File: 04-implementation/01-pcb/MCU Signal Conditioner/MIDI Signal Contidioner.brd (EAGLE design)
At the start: 78 x 31.9 mm, 26 parts, among them J2 ARDUINO-CONN-8X2, J3 ARDUINO-CONN-8X2, U4 24CS01, U6 MCP1700-SOT89, X1 SSW-107-02-S-D, X2 SSW-107-02-S-D, X3 SSW-107-02-S-D, X4 SSW-107-02-S-D, X5 MINI-USB-SHIELD-32005-201

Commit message: Update signal conditioner board.
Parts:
- moved C2 21.7 mm to (68.2, 21.8), turned to 270 degrees
- moved C1 8.01 mm to (48.4, 12.1)
- moved R9 2.04 mm to (26.2, 24.0)
- moved R7 2.03 mm to (26.2, 21.1)
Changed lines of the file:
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@@
 </element>
 <element name="U$2" library="MIDI Signal Conditioner Parts" package="74LVC4245A-SO24" value="74LVC4245A" x="56.896" y="16.129" rot="R180"/>
-<element name="C1" library="rcl" library_urn="urn:adsk.eagle:library:334" package="C0805" package3d_urn="urn:adsk.eagle:package:23617/2" value="100n" x="48.768" y="20.066" rot="R270"/>
-<element name="C2" library="rcl" library_urn="urn:adsk.eagle:library:334" package="C0805" package3d_urn="urn:adsk.eagle:package:23617/2" value="100n" x="48.768" y="12.192" rot="R90"/>
+<element name="C1" library="rcl" library_urn="urn:adsk.eagle:library:334" package="C0805" package3d_urn="urn:adsk.eagle:package:23617/2" value="100n" x="48.387" y="12.065" rot="R270"/>
+<element name="C2" library="rcl" library_urn="urn:adsk.eagle:library:334" package="C0805" package3d_urn="urn:adsk.eagle:package:23617/2" value="100n" x="68.199" y="21.844" rot="R270"/>
 <element name="R3" library="rcl" library_urn="urn:adsk.eagle:library:334" package="R0805W" package3d_urn="urn:adsk.eagle:package:23537/1" value="10K" x="19.177" y="21.082">
 <attribute name="SPICEPREFIX" value="R" x="19.177" y="21.082" size="1.778" layer="27" display="off"/>
@@
 <attribute name="SPICEPREFIX" value="R" x="43.561" y="11.557" size="1.778" layer="27" display="off"/>
 </element>
-<element name="R7" library="rcl" library_urn="urn:adsk.eagle:library:334" package="R0805W" package3d_urn="urn:adsk.eagle:package:23537/1" value="10K" x="24.13" y="21.082">
-<attribute name="SPICEPREFIX" value="R" x="24.13" y="21.082" size="1.778" layer="27" display="off"/>
+<element name="R7" library="rcl" library_urn="urn:adsk.eagle:library:334" package="R0805W" package3d_urn="urn:adsk.eagle:package:23537/1" value="10K" x="26.162" y="21.082">
+<attribute name="SPICEPREFIX" value="R" x="26.162" y="21.082" size="1.778" layer="27" display="off"/>
 </element>
 <element name="R8" library="rcl" library_urn="urn:adsk.eagle:library:334" package="R0805W" package3d_urn="urn:adsk.eagle:package:23537/1" value="20K" x="43.561" y="22.225">
 <attribute name="SPICEPREFIX" value="R" x="43.561" y="22.225" size="1.778" layer="27" display="off"/>
 </element>
-<element name="R9" library="rcl" library_urn="urn:adsk.eagle:library:334" package="R0805W" package3d_urn="urn:adsk.eagle:package:23537/1" value="10K" x="24.13" y="24.13">
-<attribute name="SPICEPREFIX" value="R" x="24.13" y="24.13" size="1.778" layer="27" display="off"/>
+<element name="R9" library="rcl" library_urn="urn:adsk.eagle:library:334" package="R0805W" package3d_urn="urn:adsk.eagle:package:23537/1" value="10K" x="26.162" y="24.003">
+<attribute name="SPICEPREFIX" value="R" x="26.162" y="24.003" size="1.778" layer="27" display="off"/>
 </element>
 <element name="R10" library="rcl" library_urn="urn:adsk.eagle:library:334" package="R0805W" package3d_urn="urn:adsk.eagle:package:23537/1" value="20K" x="43.561" y="15.113">
@@
 <contactref element="X4" pad="1"/>
 <contactref element="X4" pad="14"/>
-<wire x1="65.151" y1="20.729" x2="68.072" y2="29.464" width="0" layer="19" extent="1-1"/>
+<wire x1="68.199" y1="22.794" x2="68.072" y2="29.464" width="0" layer="19" extent="1-1"/>
+<wire x1="65.151" y1="20.729" x2="68.199" y2="22.794" width="0" layer="19" extent="1-1"/>
 <wire x1="77.343" y1="31.242" x2="68.072" y2="29.464" width="0" layer="19" extent="1-1"/>
 <wire x1="9.525" y1="26.797" x2="9.271" y2="23.048" width="0" layer="19" extent="1-1"/>
@@
 <wire x1="31.242" y1="26.924" x2="46.482" y2="29.464" width="0" layer="19" extent="1-1"/>
 <wire x1="24.765" y1="29.337" x2="31.242" y2="26.924" width="0" layer="19" extent="1-1"/>
-<wire x1="48.768" y1="11.242" x2="52.832" y2="26.924" width="0" layer="19" extent="1-1"/>
 </signal>
 <signal name="GND">
@@
 <contactref element="R6" pad="2"/>
 <contactref element="R4" pad="2"/>
-<wire x1="68.072" y1="26.924" x2="63.881" y2="20.729" width="0" layer="19" extent="1-1"/>
+<wire x1="63.881" y1="20.729" x2="68.199" y2="20.894" width="0" layer="19" extent="1-1"/>
+<wire x1="72.8619" y1="20.2641" x2="68.199" y2="20.894" width="0" layer="19" extent="1-1"/>
 <wire x1="21.854" y1="17.632" x2="19.177" y2="17.526" width="0" layer="19" extent="1-1"/>
 <wire x1="23.124" y1="17.632" x2="21.854" y2="17.632" width="0" layer="19" extent="1-1"/>
@@
 <wire x1="44.6135" y1="15.113" x2="44.6135" y2="18.669" width="0" layer="19" extent="1-1"/>
 <wire x1="44.6135" y1="11.557" x2="44.6135" y2="15.113" width="0" layer="19" extent="1-1"/>
-<wire x1="48.768" y1="19.116" x2="44.6135" y2="18.669" width="0" layer="19" extent="1-1"/>
-<wire x1="51.181" y1="20.729" x2="48.768" y2="19.116" width="0" layer="19" extent="1-1"/>
-<wire x1="52.451" y1="20.729" x2="51.181" y2="20.729" width="0" layer="19" extent="1-1"/>
-<wire x1="48.768" y1="13.142" x2="44.6135" y2="11.557" width="0" layer="19" extent="1-1"/>
-<wire x1="51.181" y1="11.529" x2="48.768" y2="13.142" width="0" layer="19" extent="1-1"/>
+<wire x1="48.387" y1="11.115" x2="44.6135" y2="11.557" width="0" layer="19" extent="1-1"/>
+<wire x1="51.181" y1="11.529" x2="48.387" y2="11.115" width="0" layer="19" extent="1-1"/>
 <wire x1="52.451" y1="11.529" x2="51.181" y2="11.529" width="0" layer="19" extent="1-1"/>
 <wire x1="53.721" y1="11.529" x2="52.451" y2="11.529" width="0" layer="19" extent="1-1"/>
@@
 <wire x1="56.261" y1="11.529" x2="54.991" y2="11.529" width="0" layer="19" extent="1-1"/>
 <wire x1="62.611" y1="11.529" x2="56.261" y2="11.529" width="0" layer="19" extent="1-1"/>
+<wire x1="51.181" y1="20.729" x2="44.6135" y2="22.225" width="0" layer="19" extent="1-1"/>
+<wire x1="52.451" y1="20.729" x2="51.181" y2="20.729" width="0" layer="19" extent="1-1"/>
 </signal>
 <signal name="+3V3">
@@
 <wire x1="38.862" y1="29.464" x2="38.862" y2="26.924" width="0.1778" layer="1"/>
 <contactref element="R7" pad="1"/>
-<wire x1="23.0775" y1="21.082" x2="38.862" y2="26.924" width="0" layer="19" extent="1-1"/>
-<wire x1="17.145" y1="26.797" x2="23.0775" y2="21.082" width="0" layer="19" extent="1-1"/>
+<wire x1="25.1095" y1="21.082" x2="38.862" y2="26.924" width="0" layer="19" extent="1-1"/>
+<wire x1="17.145" y1="26.797" x2="25.1095" y2="21.082" width="0" layer="19" extent="1-1"/>
 </signal>
 <signal name="DI4">
@@
 <wire x1="41.402" y1="29.464" x2="41.402" y2="26.924" width="0.1778" layer="1"/>
 <contactref element="R9" pad="1"/>
-<wire x1="23.0775" y1="24.13" x2="41.402" y2="26.924" width="0" layer="19" extent="1-1"/>
-<wire x1="19.685" y1="26.797" x2="23.0775" y2="24.13" width="0" layer="19" extent="1-1"/>
+<wire x1="25.1095" y1="24.003" x2="41.402" y2="26.924" width="0" layer="19" extent="1-1"/>
+<wire x1="19.685" y1="26.797" x2="25.1095" y2="24.003" width="0" layer="19" extent="1-1"/>
 </signal>
 <signal name="DO1">
@@
 <contactref element="R9" pad="2"/>
 <wire x1="43.18" y1="2.159" x2="42.5085" y2="15.113" width="0" layer="19" extent="1-1"/>
-<wire x1="25.1825" y1="24.13" x2="42.5085" y2="15.113" width="0" layer="19" extent="1-1"/>
+<wire x1="27.2145" y1="24.003" x2="42.5085" y2="15.113" width="0" layer="19" extent="1-1"/>
 </signal>
 <signal name="DI2-3V">
@@
 <contactref element="R8" pad="1"/>
 <contactref element="R7" pad="2"/>
-<wire x1="25.1825" y1="21.082" x2="42.5085" y2="22.225" width="0" layer="19" extent="1-1"/>
+<wire x1="27.2145" y1="21.082" x2="42.5085" y2="22.225" width="0" layer="19" extent="1-1"/>
 <wire x1="43.18" y1="4.699" x2="42.5085" y2="22.225" width="0" layer="19" extent="1-1"/>
 </signal>

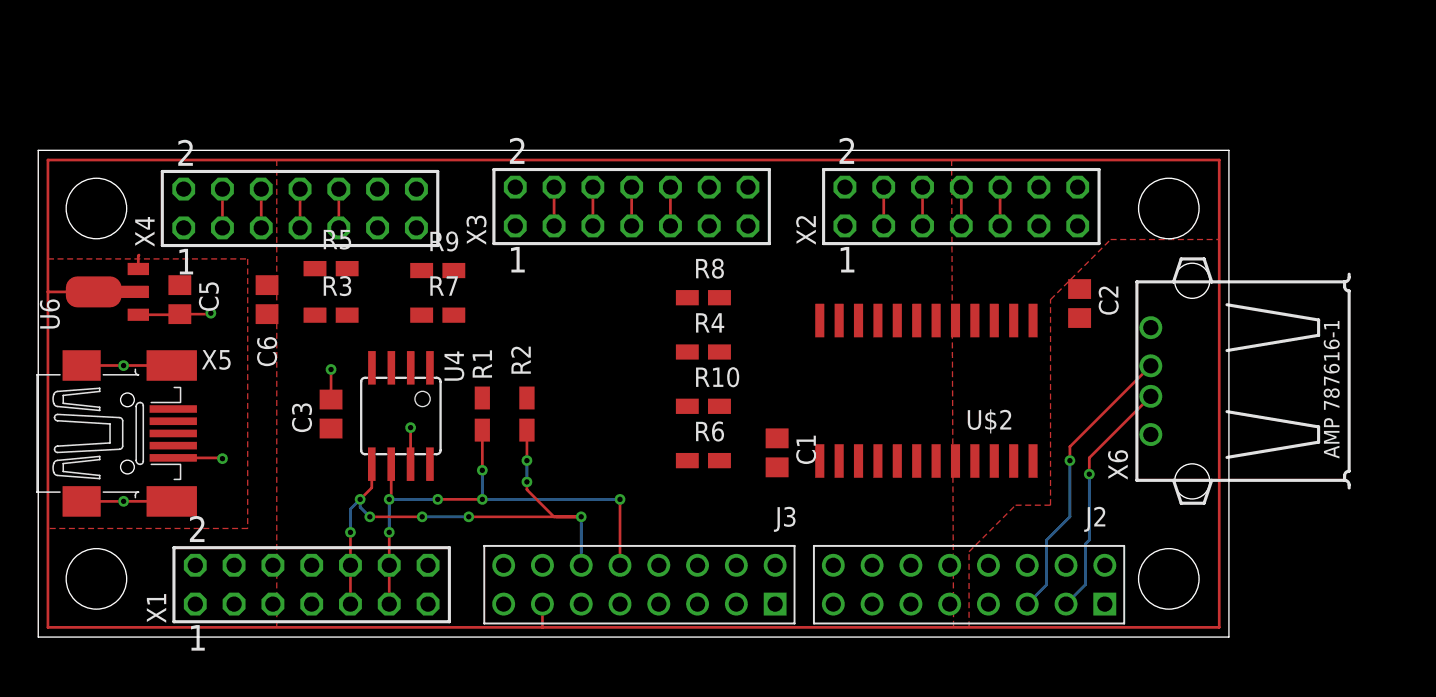
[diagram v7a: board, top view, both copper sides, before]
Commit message: Update placement of signal conditioner footprints.
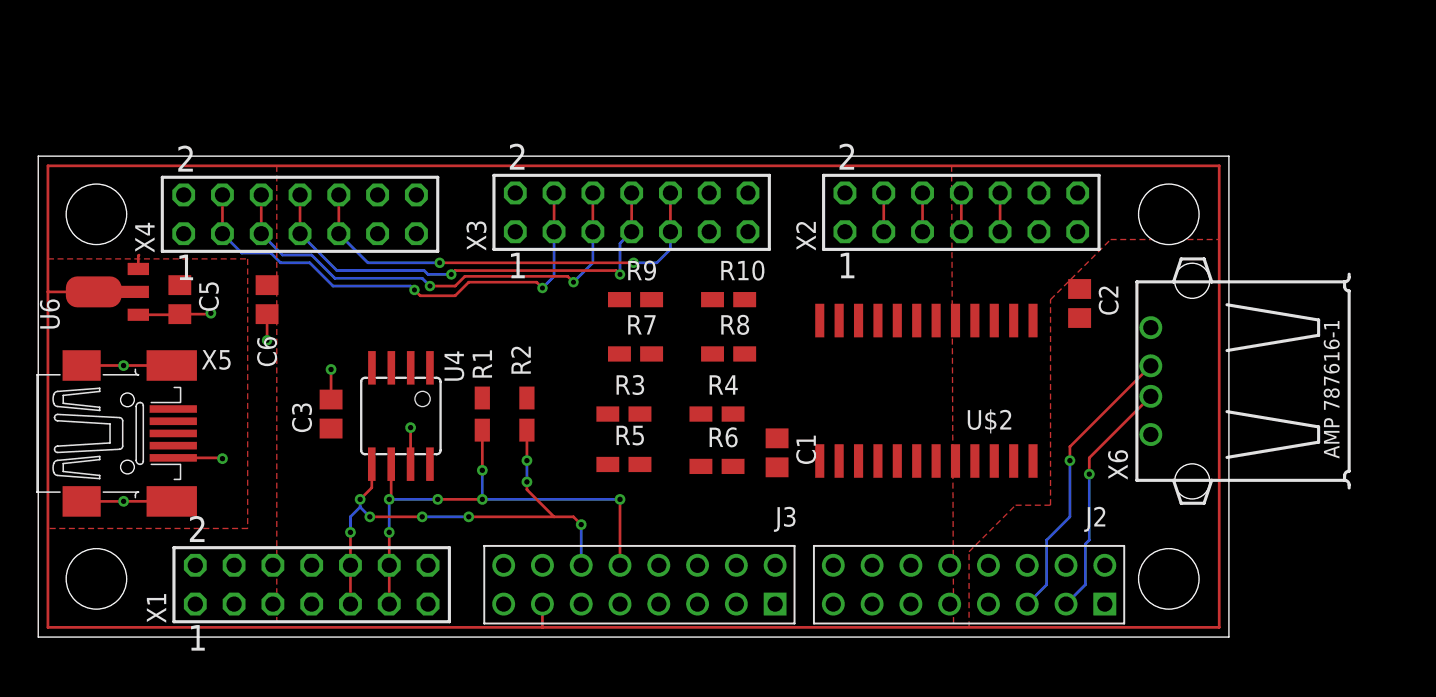
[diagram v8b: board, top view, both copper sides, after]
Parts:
- moved R5 23.1 mm to (38.4, 11.3)
- moved R3 20.2 mm to (38.4, 14.6)
- moved R7 13.2 mm to (39.1, 18.5)
- moved R9 13.1 mm to (39.1, 22.1)
- moved R10 7.18 mm to (45.2, 22.1)
- moved R4 4.16 mm to (44.5, 14.6)
- moved R8 4.04 mm to (45.2, 18.5)
- moved R6 0.97 mm to (44.5, 11.2)
- moved X2 0.38 mm to (60.5, 27.8)
- moved X3 0.38 mm to (38.9, 27.8)
- moved X4 0.38 mm to (17.1, 27.7)
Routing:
- net DI1: track 5.08 -> 32.2 mm, vias 0 -> 2
- net DI2: track 5.08 -> 31.2 mm, vias 0 -> 2
- net DI3: track 5.08 -> 30.5 mm, vias 0 -> 2
- net DI4: track 5.08 -> 29.1 mm, vias 0 -> 2
- net SDA: track 38.0 -> 33.8 mm
- net GND: track 24.3 -> 26.0 mm, vias 6 -> 7
- net +5V: track 219.2 -> 218.4 mm
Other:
- board size 78 x 31.9 mm -> 78 x 31.5 mm
